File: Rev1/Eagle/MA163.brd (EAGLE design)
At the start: 127 x 82.5 mm, 47 parts, among them IC1 Z80, IC10 74LS157N, IC11 74LS374N, IC12 74LS374N, IC13 4416, IC14 4416, IC2 2764, IC3 2764, IC4 74LS00N, IC5 74LS32N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

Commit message: Documentação
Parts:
- APPLEIIBUS1: value APPLEIIBUS2X4 -> (none)
- JMP1: value 0R-JUMPB -> (none)
- RN1: value (none) -> 3K3x10
- moved APPLEIIBUS1 0.26 mm to (97.8, 7.00)
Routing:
- net GND: track 131.0 -> 138.4 mm
- net Q3: track 194.9 -> 195.4 mm
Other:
- outline, holes or cut-outs redrawn
- board text added: "10x"

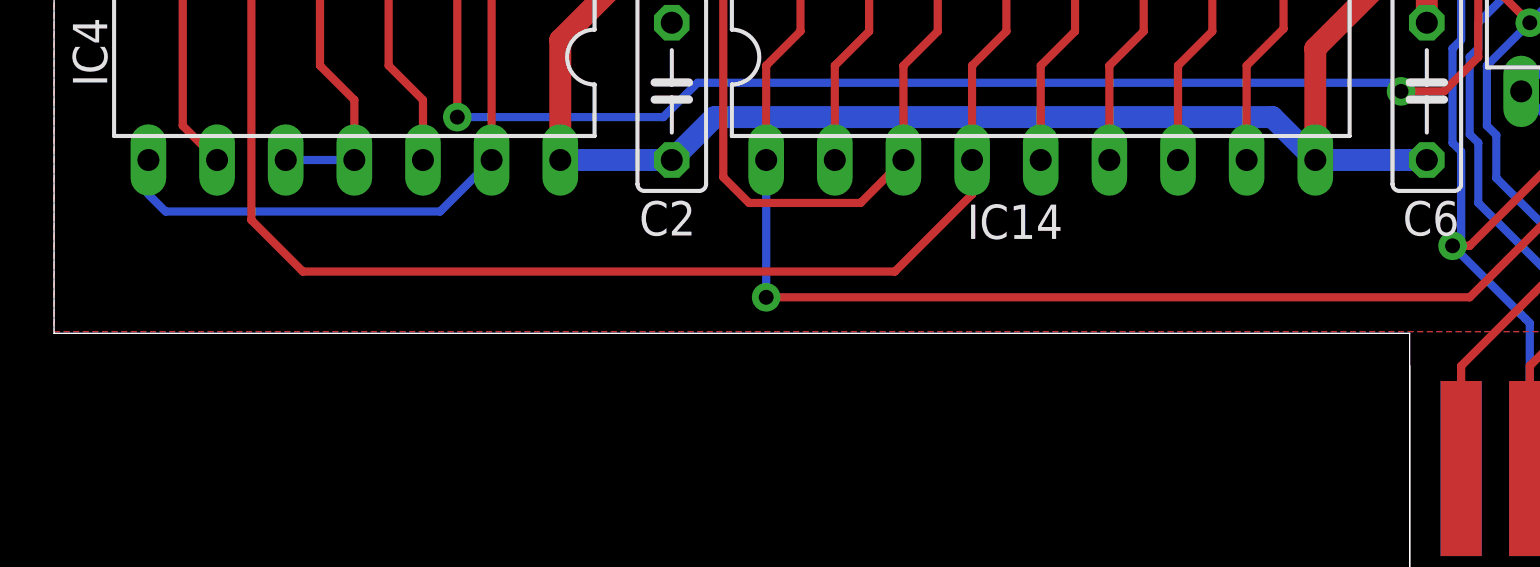
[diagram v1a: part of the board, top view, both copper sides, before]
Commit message: Adicionado silks da Microdigital e FBLabs
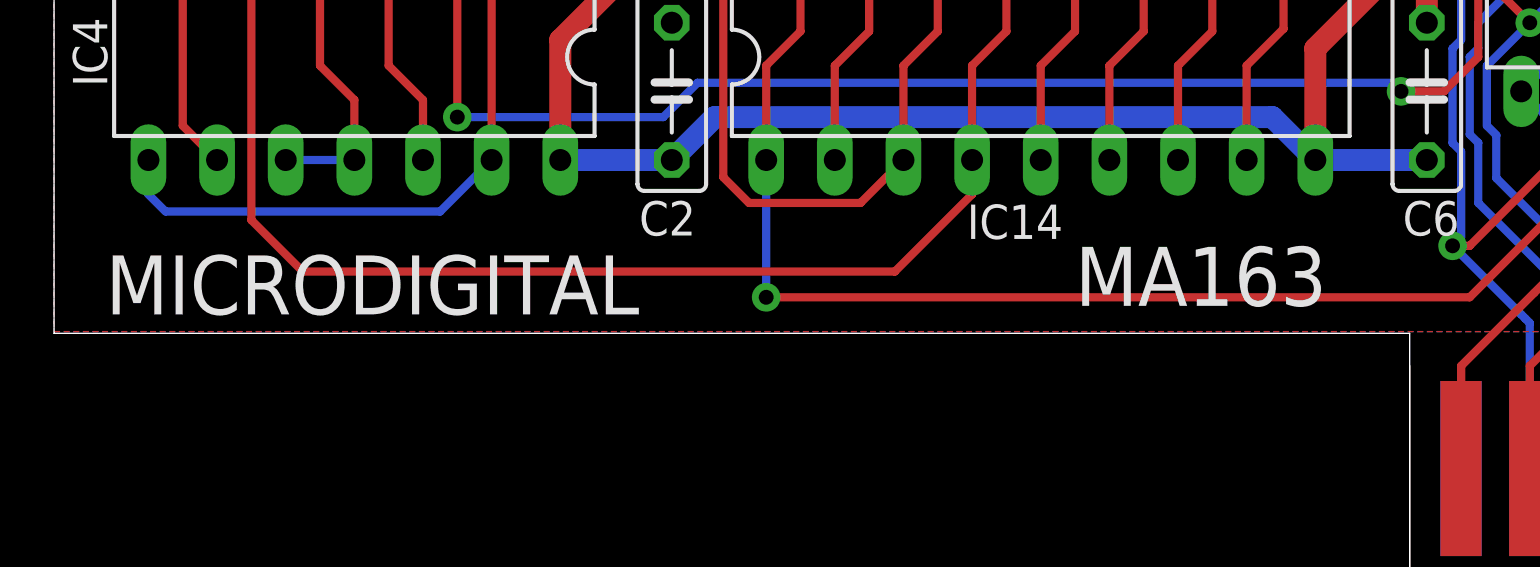
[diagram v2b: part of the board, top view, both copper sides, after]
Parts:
- added U$1: (no value), logos_fabio:LOGO_FABIO_SILK_300MIL
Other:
- board text added: "MA163"
- board text added: "MICRODIGITAL"
- board text added: "Remade by FBLabs"
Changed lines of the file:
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@@
 <drawing>
 <settings>
-<setting alwaysvectorfont="no"/>
+<setting alwaysvectorfont="yes"/>
 <setting verticaltext="up"/>
 </settings>
@@
 <wire x1="0" y1="82.55" x2="0" y2="9.4615" width="0" layer="20"/>
 <text x="101.2825" y="40.9575" size="1.27" layer="27">10x</text>
+<text x="1.905" y="10.16" size="2.1844" layer="21">MICRODIGITAL</text>
+<text x="37.7825" y="10.4775" size="2.1844" layer="21">MA163</text>
+<text x="125.73" y="66.675" size="1.778" layer="22" rot="MR270">Remade by FBLabs</text>
 </plain>
 <attributes>
@@
 <attribute name="VALUE" x="25.146" y="43.942" size="1.27" layer="27" ratio="10"/>
 </element>
+<element name="U$1" library="logos_fabio" package="LOGO_FABIO_SILK_300MIL" value="" x="125.4125" y="71.755" smashed="yes" rot="MR0"/>
 </elements>
 <signals>
